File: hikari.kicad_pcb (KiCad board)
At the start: 2 copper layers, 65 x 65 mm, 57 parts, among them CN1 USB-C, CN2 1x3, IC1 PAM2804AAB010, IC2 PAM2804AAB010, IC3 PAM2804AAB010, IC4 PAM2804AAB010, IC5 ESP-12F, IC6 CH340G, IC7 AP2112K-3.3TRG1, SW1 LS12W3-T, SW2 JS102011SAQN, T1 GSF2301, x1 12MHZ

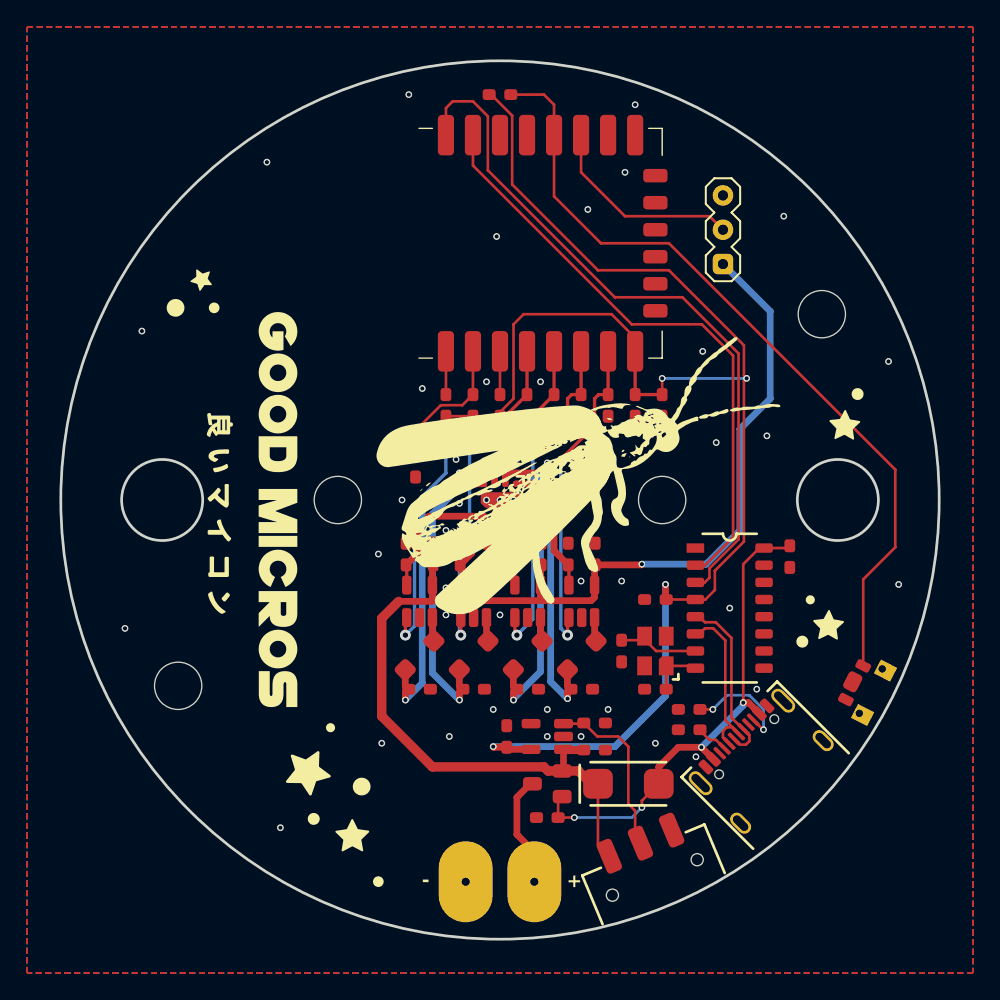
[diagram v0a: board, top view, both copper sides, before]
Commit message: added gaps on pcb under switches
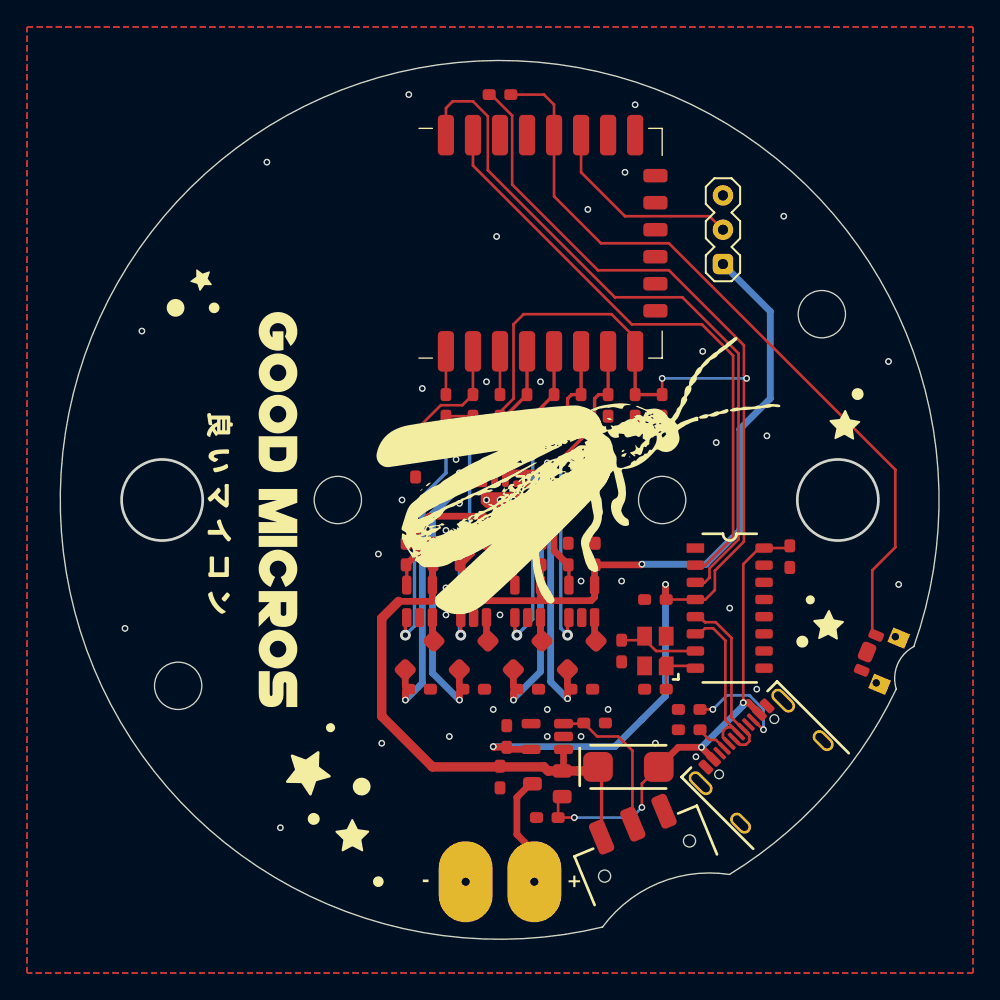
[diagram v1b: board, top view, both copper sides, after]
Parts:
- moved C9 7.28 mm to (152.4, 122.1), turned to -90 degrees
- moved SW1 2.57 mm to (180.9, 113.4), turned to -22.5 degrees
- moved SW2 1.51 mm to (163.3, 128.1), turned to 22.5 degrees
- moved D2 1.25 mm to (161.9, 121.3)
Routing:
- net 5V: track 94.9 -> 92.4 mm
- net /MCU/Button_1: track 59.4 -> 57.0 mm
- net /Power supply/Enable: track 13.1 -> 11.4 mm
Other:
- outline, holes or cut-outs redrawn

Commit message: added clearance from copper pour to pcb edge, increased soldermask openings, DRC ok
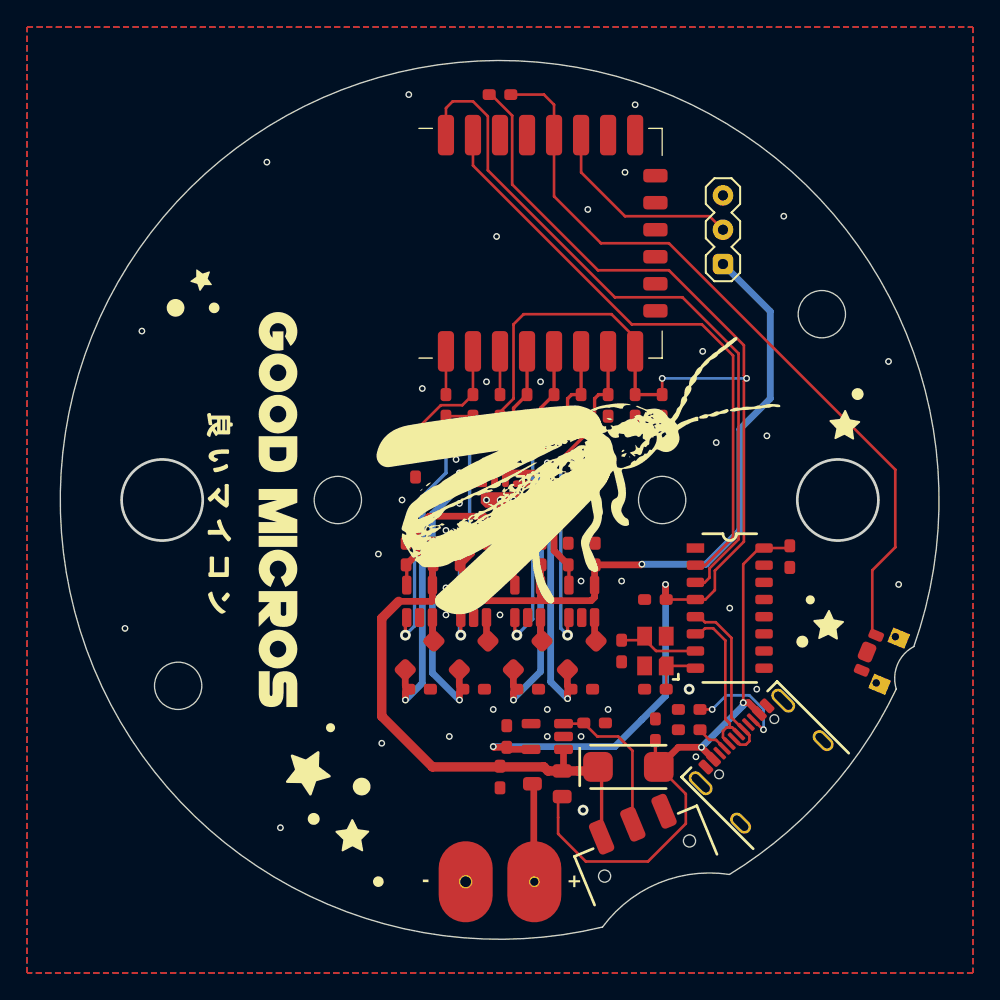
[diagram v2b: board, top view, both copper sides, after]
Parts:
- moved R5 10.3 mm to (163.9, 118.6), turned to -90 degrees
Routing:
- net /Power supply/V_USB: track 37.1 -> 46.8 mm, vias 4 -> 2
- net Net-(BAT1-+): track 8.35 -> 7.31 mm
- net /USB/DN: track 12.7 -> 11.9 mm
- net GND: vias 51 -> 52
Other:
- rule pad_to_mask_clearance: 0 -> 0.1

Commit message: fixed errors, ready for order
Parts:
- added R17: 10k, SMT:0603, F.Cu at (166.0, 76.8)
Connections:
- D1 pad 0: GND -> (no net)
- IC5 pad 10: unconnected-(IC5-IO15-Pad10) -> Net-(IC5-IO15)
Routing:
- net Net-(IC5-IO15): track 0.00 -> 9.14 mm
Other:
- outline, holes or cut-outs redrawn

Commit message: added step, preview. fixed hole diameter being documented 6 mm
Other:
- board text added: "⌀ 6.5 mm"
- board text removed: "⌀ 6 mm"
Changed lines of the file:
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@@
     (pad_to_mask_clearance 0.1)
     (allow_soldermask_bridges_in_footprints yes)
-    (grid_origin 152.4 101.6)
+    (grid_origin 152.398157 101.605455)
     (pcbplotparams
       (layerselection 0x00010fc_ffffffff)
@@
     (effects (font (size 1.5 1.5) (thickness 0.3) bold) (justify left bottom))
   )
-  (gr_text "⌀ 6 mm" (at 187.4 98.6) (layer "Dwgs.User")
+  (gr_text "⌀ 6.5 mm" (at 187.4 98.6) (layer "Dwgs.User")
     (effects (font (size 1.5 1.5) (thickness 0.3) bold) (justify left bottom))
   )
